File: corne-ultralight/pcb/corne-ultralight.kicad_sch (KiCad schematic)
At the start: 102 parts, among them J2 OLED, J7 OLED, SW1 SW_PUSH, SW10 SW_PUSH, SW11 SW_PUSH, SW12 SW_PUSH, SW13 SW_PUSH, SW14 SW_PUSH, SW15 SW_PUSH, SW16 SW_PUSH, SW17 SW_PUSH, SW18 SW_PUSH, SW19 SW_PUSH, SW2 SW_PUSH, SW20 SW_PUSH, SW21 SW_PUSH, SW22 SW_PUSH, SW23 SW_PUSH, SW24 SW_PUSH, SW25 SW_PUSH, SW26 SW_PUSH, SW27 SW_PUSH, SW28 SW_PUSH, SW29 SW_PUSH, SW3 SW_PUSH, SW30 SW_PUSH, SW31 SW_PUSH, SW32 SW_PUSH, SW33 SW_PUSH, SW34 SW_PUSH, SW35 SW_PUSH, SW36 SW_PUSH, SW37 SW_PUSH, SW38 SW_PUSH, SW39 SW_PUSH, SW4 SW_PUSH, SW40 SW_PUSH, SW41 SW_PUSH, SW42 SW_PUSH, SW5 SW_PUSH, SW6 SW_PUSH, SW7 SW_PUSH, SW8 SW_PUSH, SW9 SW_PUSH, U1 ProMicro, U2 ProMicro

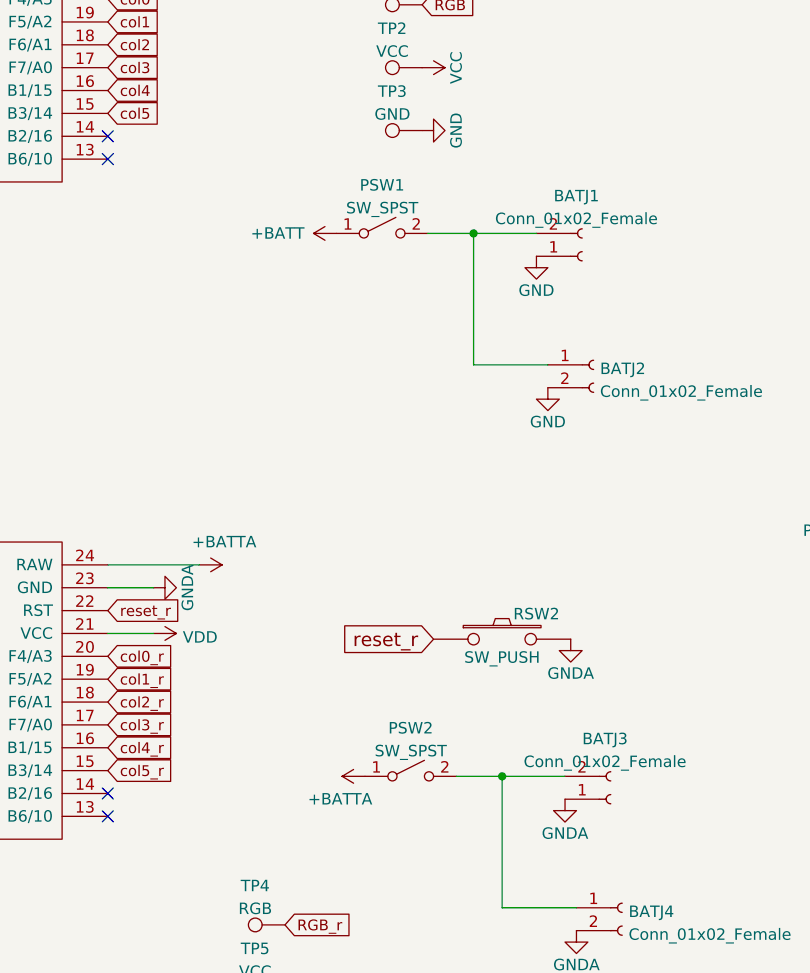
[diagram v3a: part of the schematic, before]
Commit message: Consistent power switch on/off direction.
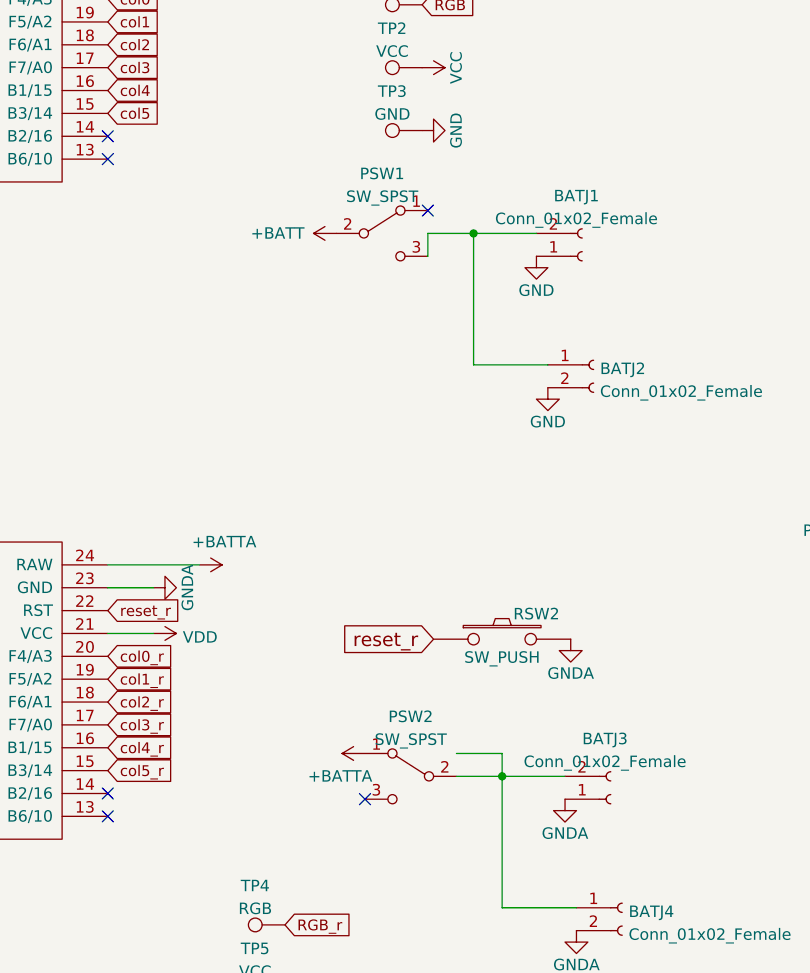
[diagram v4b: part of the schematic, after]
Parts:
- PSW1, PSW2: symbol Switch:SW_SPST -> Switch:SW_SPDT
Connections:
- net +BATT: now also PSW1.2 (B); no longer PSW1.1 (A)
- net at BATJ1.2 (Pin_2), BATJ2.1 (Pin_1): now also PSW1.3 (C); no longer PSW1.2 (B)
- no-connect marks 8 -> 10

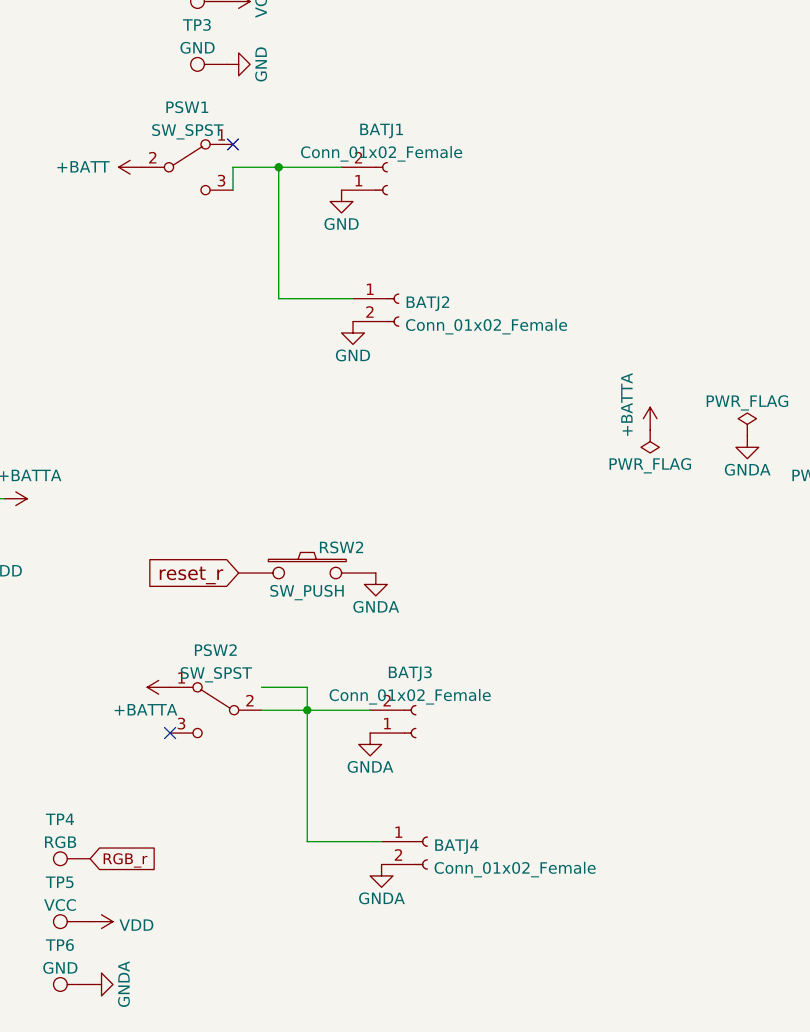
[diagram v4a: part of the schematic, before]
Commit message: feat: switch to hotswap
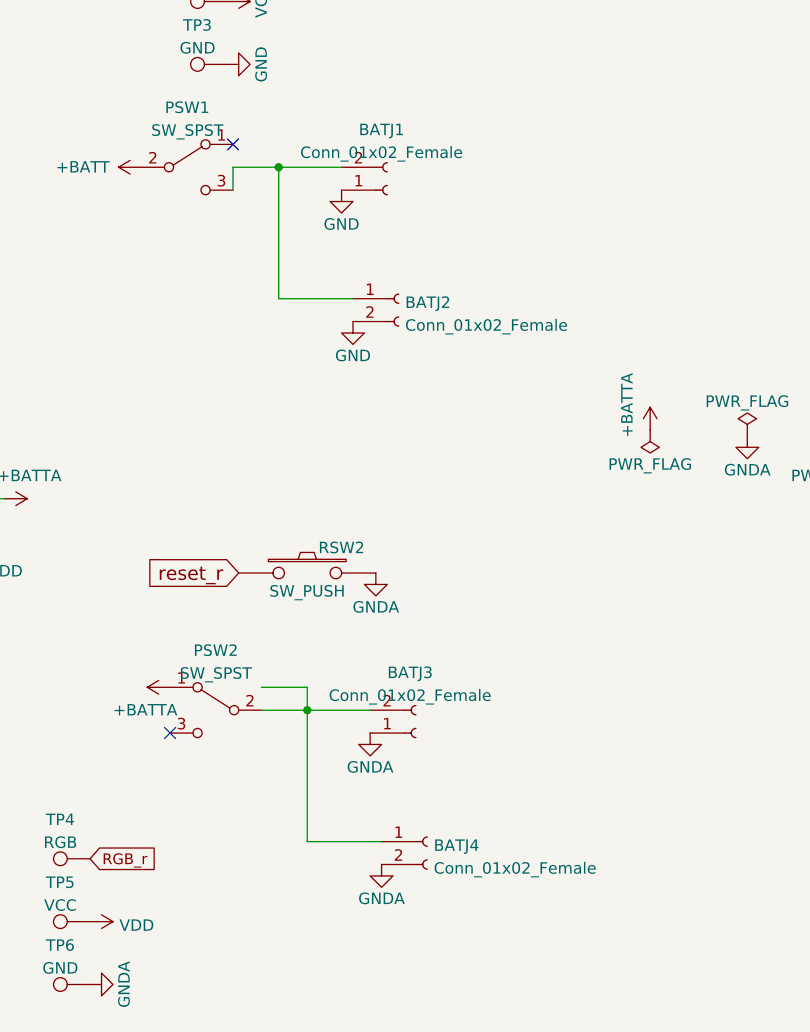
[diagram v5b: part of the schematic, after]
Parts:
- SW1, SW10, SW11, SW12, SW13, SW14, SW15, SW16, SW17, SW18, SW19, SW2, SW20, SW22, SW23, SW24, SW25, SW26, SW27, SW28, SW29, SW3, SW30, SW31, SW32, SW33, SW34, SW35, SW36, SW37, SW38, SW39, SW4, SW40, SW41, SW5, SW6, SW7, SW8, SW9: footprint gateron-ks27:gateron-ks27-choc-v1 -> PCM_Switch_Keyboard_Hotswap_Kailh:SW_Hotswap_Kailh_Choc_V1V2
- SW21, SW42: footprint gateron-ks27:gateron-ks27-choc-v1-1.5u -> PCM_Switch_Keyboard_Hotswap_Kailh:SW_Hotswap_Kailh_Choc_V1V2_1.50u
